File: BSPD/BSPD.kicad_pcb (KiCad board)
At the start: 2 copper layers, 102.9 x 124.7 mm, 55 parts, among them J1 DT13-48PABCD-R015, K1 Latching Relay, Q2 STS6NF20V, Q3 STS6NF20V, U1 4081, U10 DK1A1B-12V, U11 TLP3122AE, U12 OP AMP, U13 LM7805_TO220, U14 ISO1050DUB, U15 LM7809_TO220, U2 OP AMP, U3 OP AMP, U4 NUCLEO-L432KC, U5 2x4 OR GATE, U6 LM555N, U7 TLP3122AE, U9 74LVC1GU04DRL

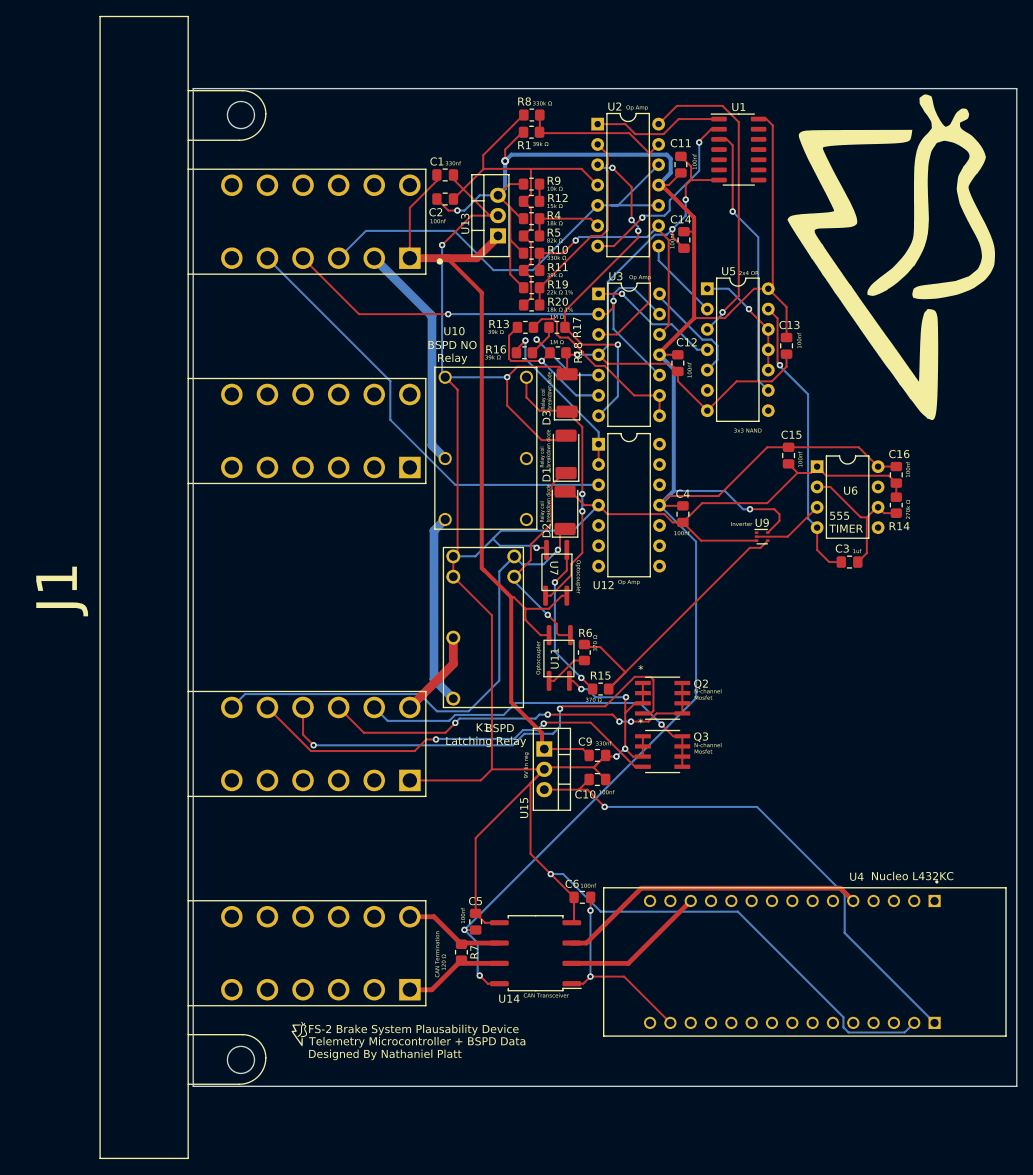
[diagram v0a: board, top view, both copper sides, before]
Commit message: bspd inverter -> nand gate (larger)
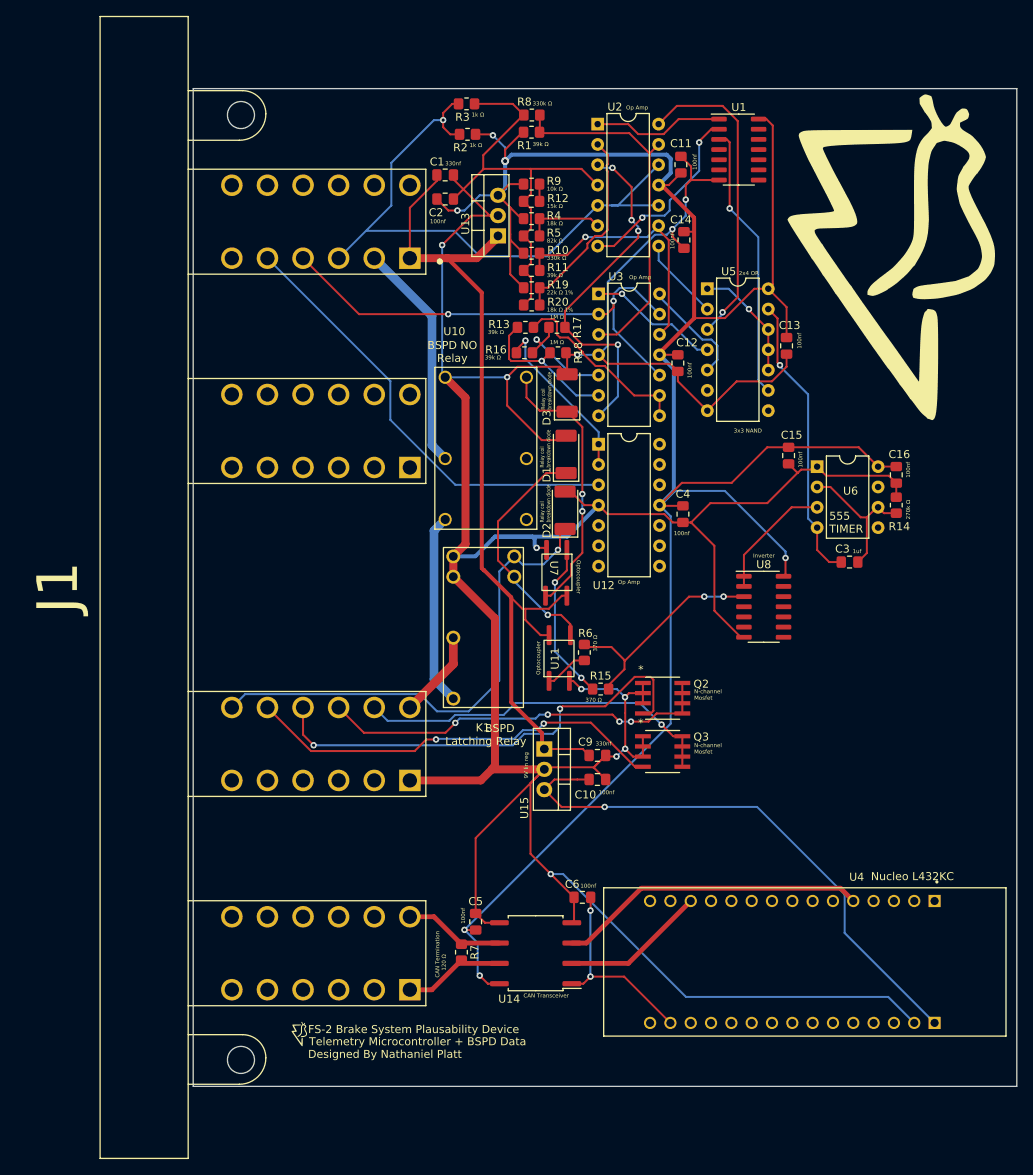
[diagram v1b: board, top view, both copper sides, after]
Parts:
- removed U9: 74LVC1GU04DRL, Package_TO_SOT_SMD:SOT-553
- added R2: 1k, Resistor_SMD:R_0805_2012Metric_Pad1.20x1.40mm_HandSolder, F.Cu at (61.3, 28.6)
- added R3: 1k, Resistor_SMD:R_0805_2012Metric_Pad1.20x1.40mm_HandSolder, F.Cu at (61.2, 24.8)
- added U8: HEF4093B, Package_SO:SOIC-14_3.9x8.7mm_P1.27mm, F.Cu at (98.4, 87.6)
- C10: value 0.33µF -> 100nf
- C5, C6: value 100nF -> 100nf
- C9: value 0.33µF -> 330nf
- R15, R6: value 370 -> 374
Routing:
- net /Brake Output: track 54.8 -> 78.4 mm, vias 0 -> 1
- net GND: track 486.8 -> 500.0 mm
- net /BSPD Fault Post Timer: track 36.7 -> 28.1 mm, vias 0 -> 2
- net Net-(U6-Q): track 9.09 -> 15.6 mm
- net +5V: track 289.9 -> 296.3 mm, vias 5 -> 6
- net +9V: track 65.5 -> 69.8 mm
- net Net-(D1-K): track 26.8 -> 29.9 mm
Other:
- board text added: "1k Ω"

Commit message: backed up stuff? and fixed opamps being backward (power supply)
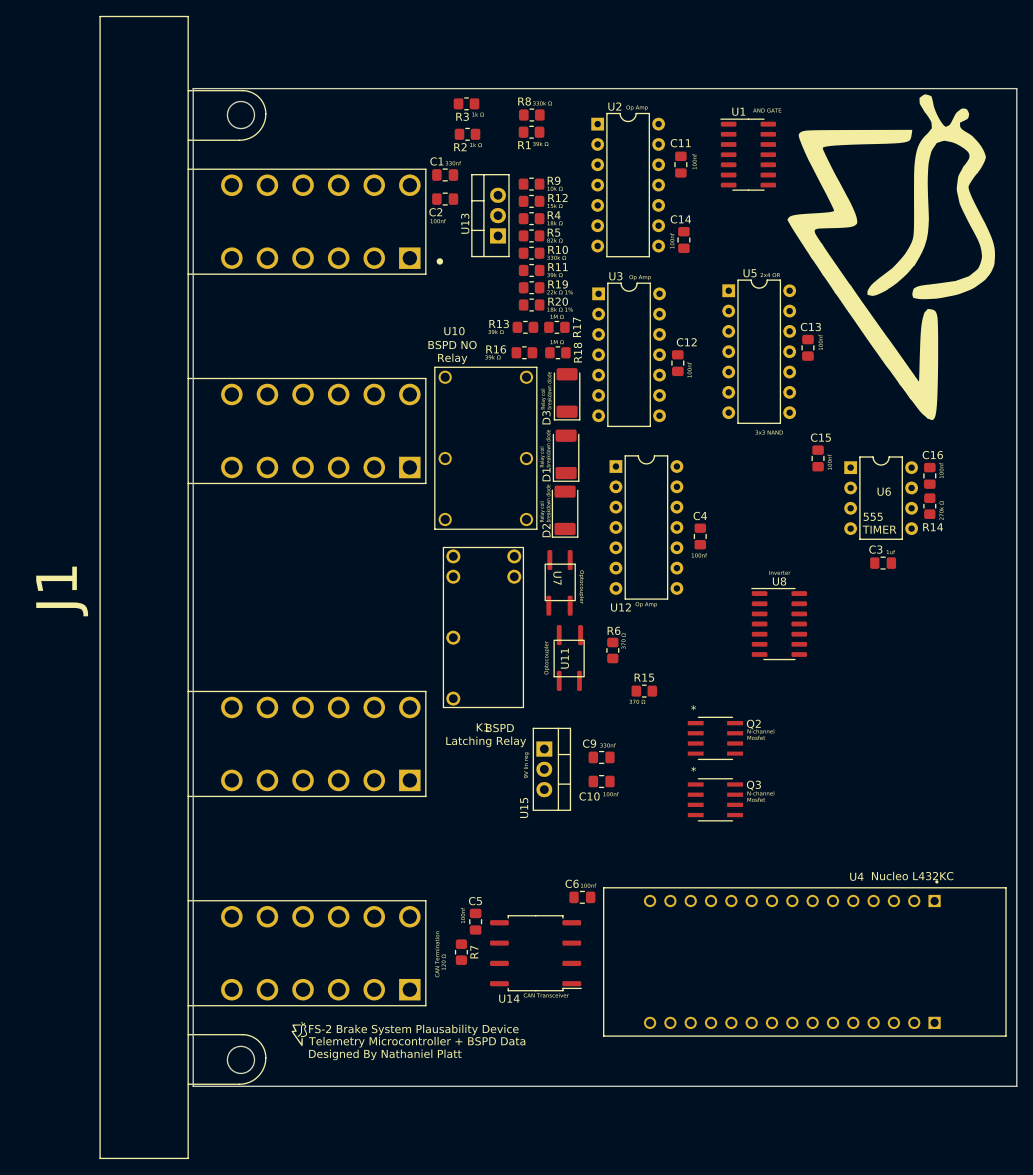
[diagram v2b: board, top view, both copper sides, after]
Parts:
- moved Q3 8.95 mm to (92.3, 111.8)
- moved Q2 8.30 mm to (92.3, 104.1)
- moved R15 5.47 mm to (83.4, 98.2)
- moved C16 4.19 mm to (119.1, 71.3)
- moved C3 4.19 mm to (113.3, 82.2)
- moved R14 4.19 mm to (119.1, 75.1)
- moved U6 4.19 mm to (109.2, 70.2)
- moved C15 3.70 mm to (105.2, 69.1)
- moved R6 3.57 mm to (79.5, 93.1)
- moved C4 3.53 mm to (90.4, 78.8)
- moved U12 3.53 mm to (79.9, 70.1)
- moved U8 2.92 mm to (100.3, 89.8)
- moved C13 2.69 mm to (103.9, 55.3)
- moved U5 2.69 mm to (94.0, 48.1)
- moved U1 1.36 mm to (96.5, 31.1)
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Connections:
- K1 pad 5: Net-(D1-K) -> /SH_RESET
- K1 pad 6: /SH_RESET -> Net-(D1-K)
- U12 pad 11: +5V -> GND
- U12 pad 4: GND -> +5V
- U2 pad 11: +5V -> GND
- U2 pad 4: GND -> +5V
- U3 pad 11: +5V -> GND
- U3 pad 4: GND -> +5V
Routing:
- net GND: track 500.0 -> 0.00 mm, vias 11 -> 0
- net +5V: track 296.3 -> 0.00 mm, vias 6 -> 0
- net +12V: track 109.8 -> 0.00 mm
- net /Brake Output: track 78.4 -> 0.00 mm, vias 1 -> 0
- net +9V: track 69.8 -> 0.00 mm, vias 1 -> 0
- net /Current Output: track 62.8 -> 0.00 mm, vias 2 -> 0
- net /SH_RESET: track 62.7 -> 0.00 mm, vias 1 -> 0
- net /BMS_FAULT 5V: track 58.1 -> 0.00 mm, vias 2 -> 0
- net /Current Vref: track 56.0 -> 0.00 mm
- net /IMD_FAULT 5V: track 52.9 -> 0.00 mm, vias 2 -> 0
- net /BMS Light Low Side: track 49.8 -> 0.00 mm, vias 4 -> 0
- net /IMD Light Low Side: track 45.7 -> 0.00 mm, vias 1 -> 0
- net /4.5V: track 45.2 -> 0.00 mm
- net /Current Sensor Differential: track 44.5 -> 0.00 mm, vias 4 -> 0
- net /BrkSenShort: track 39.2 -> 0.00 mm, vias 1 -> 0
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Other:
- board text added: "AND GATE"

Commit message: Retraced everything to fix opamps
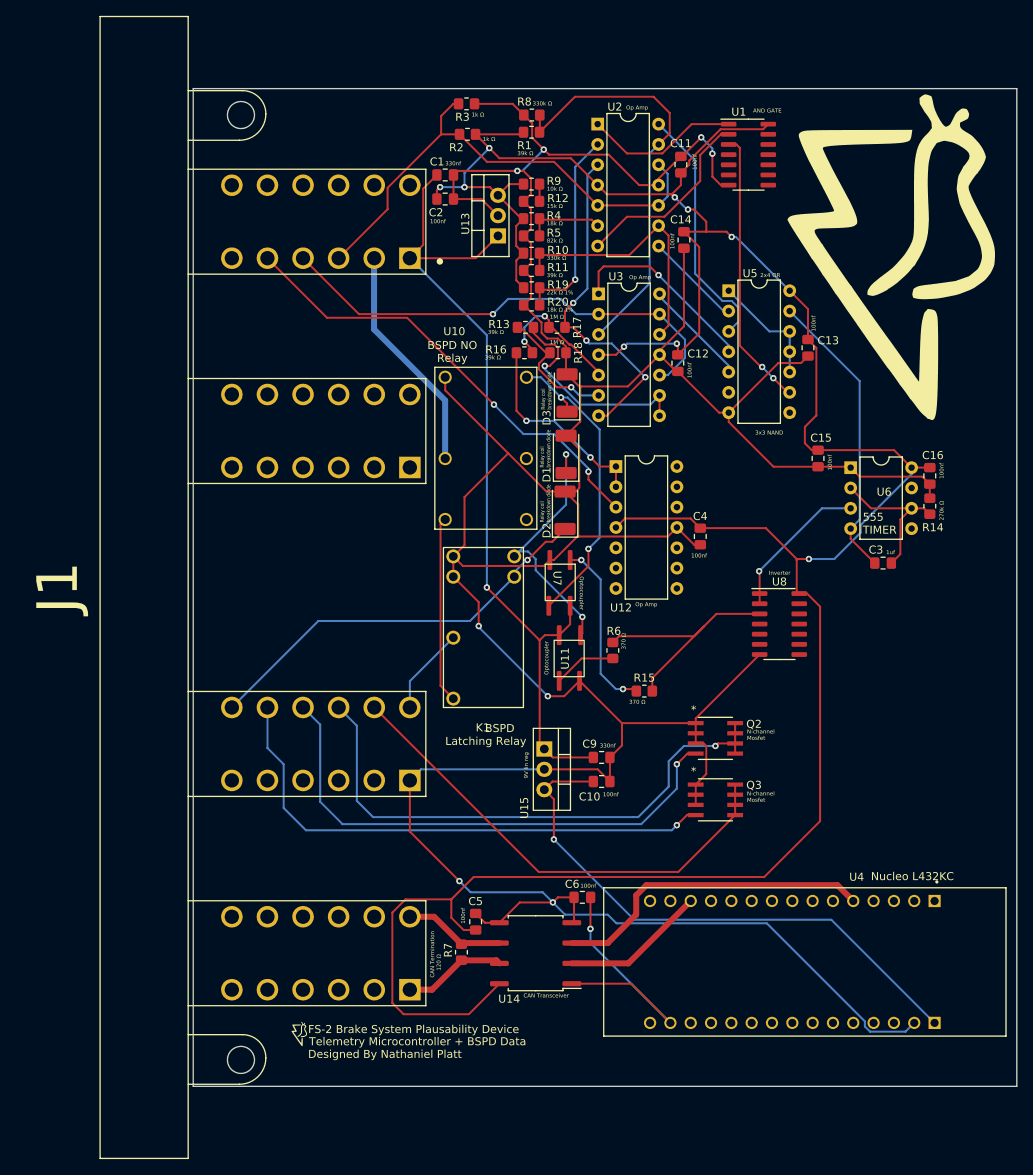
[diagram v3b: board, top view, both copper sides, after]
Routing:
- net GND: track 0.00 -> 476.9 mm, vias 0 -> 8
- net +5V: track 0.00 -> 346.0 mm, vias 0 -> 9
- net +12V: track 0.00 -> 105.8 mm, vias 0 -> 1
- net +9V: track 0.00 -> 70.4 mm, vias 0 -> 1
- net /BMS Light Low Side: track 0.00 -> 70.2 mm, vias 0 -> 1
- net /IMD_FAULT 5V: track 0.00 -> 66.9 mm, vias 0 -> 1
- net /BMS_FAULT 5V: track 0.00 -> 66.2 mm, vias 0 -> 1
- net /Brake Output: track 0.00 -> 62.8 mm
- net /IMD Light Low Side: track 0.00 -> 60.4 mm
- net /Current Output: track 0.00 -> 59.9 mm, vias 0 -> 1
- net /Current Vref: track 0.00 -> 57.3 mm, vias 0 -> 2
- net /4.5V: track 0.00 -> 52.5 mm
- net /SH_RESET: track 0.00 -> 51.2 mm, vias 0 -> 1
- net /Current Sensor Differential: track 0.00 -> 42.5 mm, vias 0 -> 3
- net /CAN1_TD: track 0.00 -> 40.4 mm
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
